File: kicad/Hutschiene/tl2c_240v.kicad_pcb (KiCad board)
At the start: 2 copper layers, 82 x 58.4 mm, 23 parts, among them P106 240VAC, P107 LED_DRIVER, P108 LED_OUT, Q401 IRLML2502, Q402 IRLML2502, Q403 IRLML2502

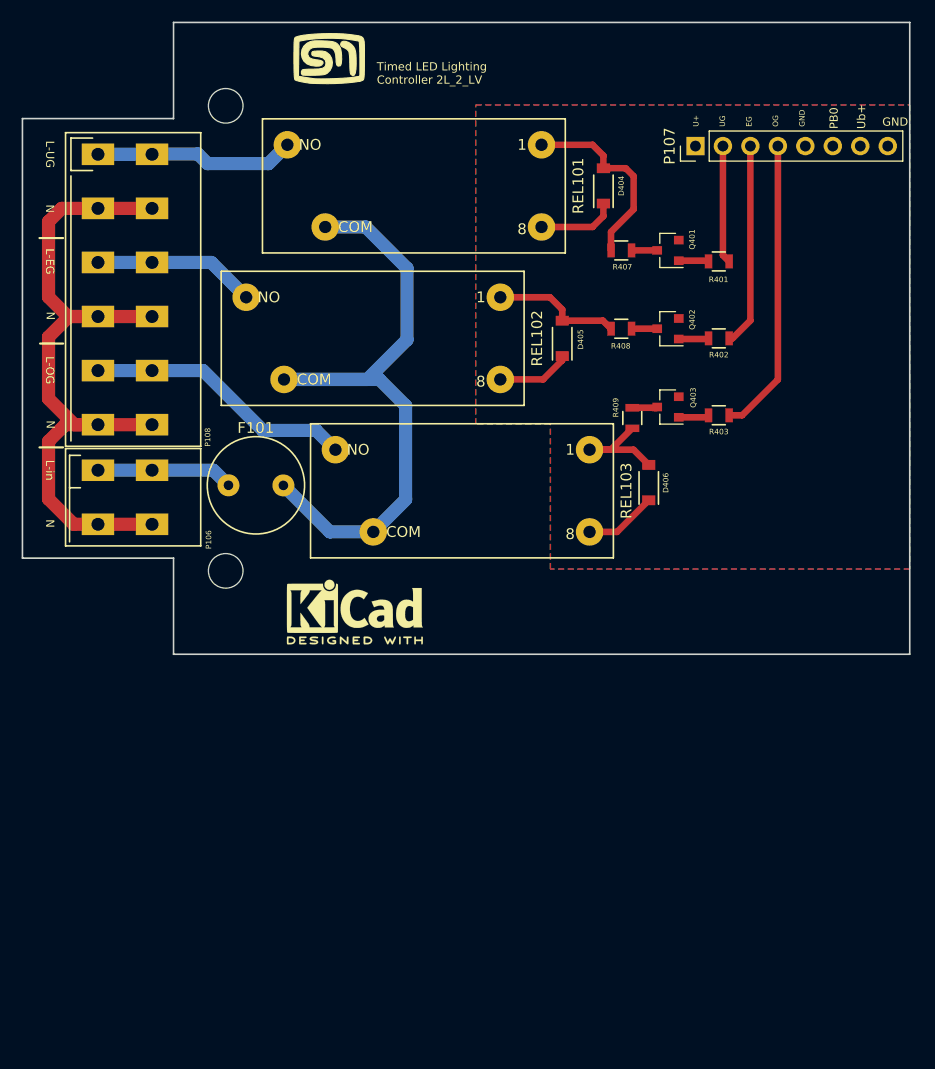
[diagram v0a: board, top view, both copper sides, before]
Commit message: Adjusted the size and location of the terminal blocks
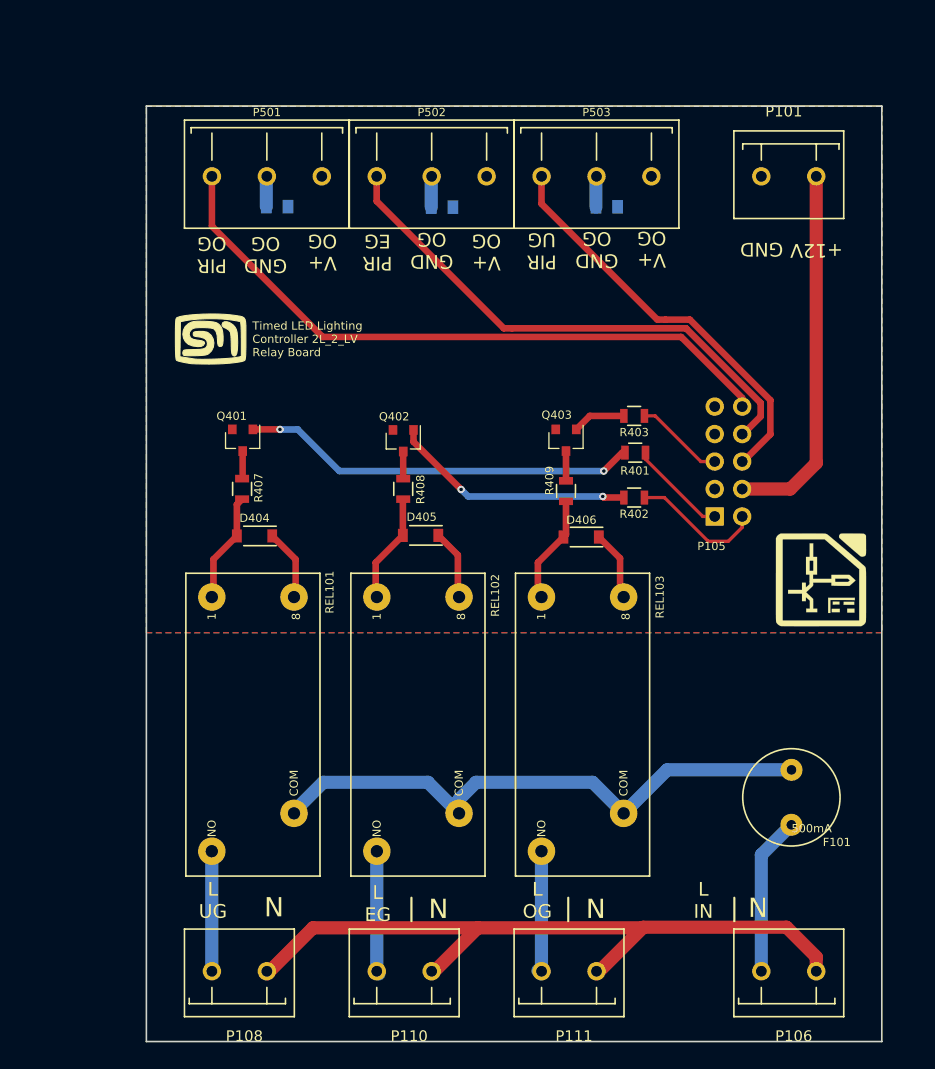
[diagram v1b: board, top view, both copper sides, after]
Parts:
- removed P107: LED_DRIVER, Pin_Headers:Pin_Header_Straight_1x08_Pitch2.54mm
- removed REF** (x2): MountingHole_3.2mm_M3, Mounting_Holes:MountingHole_3.2mm_M3
- removed REF***: KiCad-Logo2_6mm_SilkScreen, Symbols:KiCad-Logo2_6mm_SilkScreen
- added C501: 100nF 50V, Capacitors_SMD:C_0805, B.Cu at (57.8, 69.1)
- added C502: 100nF 50V, Capacitors_SMD:C_0805, B.Cu at (88.3, 69.1)
- added C503: 100nF 50V, Capacitors_SMD:C_0805, B.Cu at (73.1, 69.2)
- added G***: LOGO, tl2c-footprint:KiCad_LOGO_9mm, F.Cu at (108.1, 103.5)
- added P101: 12VDC, tl2c-footprint:PCB_Screw_Terminal_Block_5.08mm_x_2, F.Cu at (107.7, 66.3)
- added P105: DRV CONN, Pin_Headers:Pin_Header_Straight_2x05_Pitch2.54mm, B.Cu at (98.3, 97.8)
- added P110: EG, tl2c-footprint:PCB_Screw_Terminal_Block_5.08mm_x_2, F.Cu at (67.0, 139.8)
- added P111: OG, tl2c-footprint:PCB_Screw_Terminal_Block_5.08mm_x_2, F.Cu at (82.3, 139.8)
- added P501: CONN_PIR_OG, tl2c-footprint:PCB_Screw_Terminal_Block_5.8mm_x_3, F.Cu at (56.9, 66.3)
- added P502: CONN_PIR_EG, tl2c-footprint:PCB_Screw_Terminal_Block_5.8mm_x_3, F.Cu at (72.1, 66.3)
- added P503: CONN_PIR_UG, tl2c-footprint:PCB_Screw_Terminal_Block_5.8mm_x_3, F.Cu at (87.4, 66.3)
- P106: footprint tl2c-footprint:TERMINAL_BLOCK_2_5MM_5MM -> tl2c-footprint:PCB_Screw_Terminal_Block_5.08mm_x_2
- P108: value LED_OUT -> UG; footprint tl2c-footprint:TERMINAL_BLOCK_6_5MM_5MM -> tl2c-footprint:PCB_Screw_Terminal_Block_5.08mm_x_2
- moved P106 76.9 mm to (102.6, 139.8)
- moved P108 76.3 mm to (51.8, 139.8)
- moved F101 57.3 mm to (105.4, 123.7), turned to 90 degrees
- moved REL101 52.0 mm to (55.6, 117.0), turned to 90 degrees
- moved D404 45.7 mm to (55.8, 99.5), turned to 180 degrees
- moved Q401 43.1 mm to (54.6, 90.7), turned to 270 degrees
- moved R407 41.4 mm to (54.6, 95.2), turned to 90 degrees
- moved REL102 36.0 mm to (70.9, 117.0), turned to 90 degrees
- moved G*** 28.1 mm to (51.6, 81.3)
- moved Q402 26.6 mm to (69.5, 90.8), turned to 270 degrees
- moved R408 25.0 mm to (69.5, 95.2), turned to 90 degrees
- moved REL103 24.3 mm to (86.1, 117.0), turned to 90 degrees
- moved D405 22.4 mm to (71.1, 99.5), turned to 180 degrees
- moved R401 19.3 mm to (91.0, 91.8)
- moved R402 16.7 mm to (90.8, 96.0)
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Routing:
- net /PIR_Connector/PIR_OG: track 0.00 -> 61.0 mm
- net /PIR_Connector/PIR_EG: track 0.00 -> 49.7 mm
- net /PIR_Connector/PIR_UG: track 0.00 -> 38.5 mm
- net /DRV_PWR_IN: track 0.00 -> 34.4 mm
- net Net-(Q401-Pad1): track 2.78 -> 36.7 mm, vias 0 -> 2
- net Net-(Q402-Pad1): track 2.77 -> 22.7 mm, vias 0 -> 2
- net /LED Driver/Relay_OG: track 27.5 -> 8.25 mm
- net /LineOG: track 25.0 -> 11.5 mm
- net Net-(F101-Pad2): track 64.0 -> 53.3 mm
- net GNDA: track 0.00 -> 8.53 mm
- net Net-(D404-Pad2): track 18.0 -> 10.2 mm
- net /LineUG: track 18.6 -> 11.1 mm
- net /LED Driver/Relay_EG: track 18.8 -> 12.3 mm
- net /LineEG: track 15.3 -> 11.5 mm
- net /Neutral: track 70.1 -> 67.4 mm
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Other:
- board size 82 x 58.4 mm -> 68 x 86.5 mm
- copper layers 2 -> 4
- board text added: "+12V"
- board text added: "500mA"
- board text added: "GND OG"
- board text added: "L EG"
- board text added: "L IN"
- board text added: "L OG"
- board text added: "L UG"
- board text added: "PIR EG"
- board text added: "PIR OG"
- board text added: "PIR UG"
- board text added: "Timed LED Lighting Controller 2L_2_LV Relay Board"
- board text added: "V+ OG"
- board text removed: "L-EG"
- board text removed: "L-OG"
- board text removed: "L-UG"
- board text removed: "L-in"
- board text removed: "PB0"
- board text removed: "Timed LED Lighting Controller 2L_2_LV"
- board text removed: "U+ UG EG OG GND"
- board text removed: "Ub+"

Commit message: Pushed the boards to OSHPark
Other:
- copper layers 4 -> 2
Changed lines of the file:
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@@
     (links 51)
     (no_connects 0)
-    (area 20.250001 40.4 248.26 176.820001)
+    (area 45.674999 59.724999 113.825001 146.375001)
     (thickness 1.6)
     (drawings 62)
@@
   (layers
     (0 F.Cu signal)
-    (1 Ub+ power)
-    (2 U+ power)
     (31 B.Cu signal)
     (32 B.Adhes user)
@@
     (40 Dwgs.User user)
     (41 Cmts.User user)
-    (42 Eco1.User user)
-    (43 Eco2.User user)
+    (42 Eco1.User user hide)
+    (43 Eco2.User user hide)
     (44 Edge.Cuts user)
     (45 Margin user)
@@
     (at 105.39 123.72 90)
     (tags "Fuse, ESKA")
-    (fp_text reference F101 (at -4.15 4.2 180) (layer F.SilkS)
+    (fp_text reference F101 (at -4.37 5.06 180) (layer F.SilkS)
       (effects (font (size 0.762 0.762) (thickness 0.127)))
     )
@@
   (module tl2c-footprint:PCB_Screw_Terminal_Block_5.8mm_x_3 (layer F.Cu)
     (at 56.89 66.3 180)
-    (fp_text reference P501 (at 0 5.92 180) (layer F.SilkS)
+    (fp_text reference P501 (at 0.01 5.76 180) (layer F.SilkS)
       (effects (font (size 0.762 0.762) (thickness 0.127)))
     )
@@
   (module tl2c-footprint:PCB_Screw_Terminal_Block_5.8mm_x_3 (layer F.Cu)
     (at 72.13 66.3 180)
-    (fp_text reference P502 (at 0 5.92 180) (layer F.SilkS)
+    (fp_text reference P502 (at 0.01 5.76 180) (layer F.SilkS)
       (effects (font (size 0.762 0.762) (thickness 0.127)))
     )
@@
   (module tl2c-footprint:PCB_Screw_Terminal_Block_5.8mm_x_3 (layer F.Cu)
     (at 87.37 66.3 180)
-    (fp_text reference P503 (at 0 5.92 180) (layer F.SilkS)
+    (fp_text reference P503 (at 0.08 5.76 180) (layer F.SilkS)
       (effects (font (size 0.762 0.762) (thickness 0.127)))
     )
@@
   (module tl2c-footprint:PCB_Screw_Terminal_Block_5.08mm_x_2 (layer F.Cu)
     (at 102.61 139.8)
-    (fp_text reference P106 (at 3 6) (layer F.SilkS)
+    (fp_text reference P106 (at 3.08 5.06) (layer F.SilkS)
       (effects (font (size 1 1) (thickness 0.15)))
     )
@@
   (module tl2c-footprint:PCB_Screw_Terminal_Block_5.08mm_x_2 (layer F.Cu)
     (at 51.81 139.8)
-    (fp_text reference P108 (at 3 6) (layer F.SilkS)
+    (fp_text reference P108 (at 2.48 5.06) (layer F.SilkS)
       (effects (font (size 1 1) (thickness 0.15)))
     )
@@
   (module tl2c-footprint:PCB_Screw_Terminal_Block_5.08mm_x_2 (layer F.Cu)
     (at 67.05 139.8)
-    (fp_text reference P110 (at 3 6) (layer F.SilkS)
+    (fp_text reference P110 (at 3.05 5.09) (layer F.SilkS)
       (effects (font (size 1 1) (thickness 0.15)))
     )
@@
   (module tl2c-footprint:PCB_Screw_Terminal_Block_5.08mm_x_2 (layer F.Cu)
     (at 82.29 139.8)
-    (fp_text reference P111 (at 3 6) (layer F.SilkS)
+    (fp_text reference P111 (at 3.05 4.98) (layer F.SilkS)
       (effects (font (size 1 1) (thickness 0.15)))
     )
@@
   (module tl2c-footprint:PCB_Screw_Terminal_Block_5.08mm_x_2 (layer F.Cu)
     (at 107.69 66.3 180)
-    (fp_text reference P101 (at 3 6 180) (layer F.SilkS)
+    (fp_text reference P101 (at 2.42 5 180) (layer F.SilkS)
       (effects (font (size 1 1) (thickness 0.15)))
     )
@@
     (arrow2b (pts (xy 28.25 59.8) (xy 28.836421 60.926504)))
   )
-  (gr_text 500mA (at 105.4 126.6) (layer F.SilkS)
+  (gr_text 500mA (at 103.9 118.53) (layer F.SilkS)
     (effects (font (size 0.762 0.762) (thickness 0.127)) (justify left))
   )
-  (gr_text GND (at 102.64 73.04 180) (layer F.SilkS)
+  (gr_text GND (at 102.45 71.36 180) (layer F.SilkS)
     (effects (font (size 1.27 1.27) (thickness 0.1778)))
   )
-  (gr_text +12V (at 107.71 73.15 180) (layer F.SilkS)
+  (gr_text +12V (at 108.17 71.21 180) (layer F.SilkS)
     (effects (font (size 1.27 1.27) (thickness 0.1778)))
   )
@@
     (effects (font (size 1.27 1.27) (thickness 0.1778)))
   )
-  (gr_text "L\nIN" (at 97.25 133.25) (layer F.SilkS)
+  (gr_text "L\nIN" (at 102.4 133.25) (layer F.SilkS)
     (effects (font (size 1.27 1.27) (thickness 0.1778)))
   )
@@
     (effects (font (size 1.27 1.27) (thickness 0.1778)))
   )
-  (gr_text N (at 102.3 133.95) (layer F.SilkS)
+  (gr_text N (at 107.54 134.06) (layer F.SilkS)
     (effects (font (size 1.778 1.778) (thickness 0.254)))
   )
@@
   (gr_line (start 45.75 146.3) (end 45.75 59.8) (angle 90) (layer Edge.Cuts) (width 0.15))
   (gr_line (start 70.259 133.0008) (end 70.259 135.1852) (angle 90) (layer F.SilkS) (width 0.2))
-  (gr_line (start 100.1138 133.0008) (end 100.1138 135.1852) (angle 90) (layer F.SilkS) (width 0.2))
+  (gr_line (start 105.1138 132.9208) (end 105.1138 135.1052) (angle 90) (layer F.SilkS) (width 0.2))
   (gr_text "L\nEG" (at 67.15 133.55) (layer F.SilkS)
     (effects (font (size 1.27 1.27) (thickness 0.1778)))

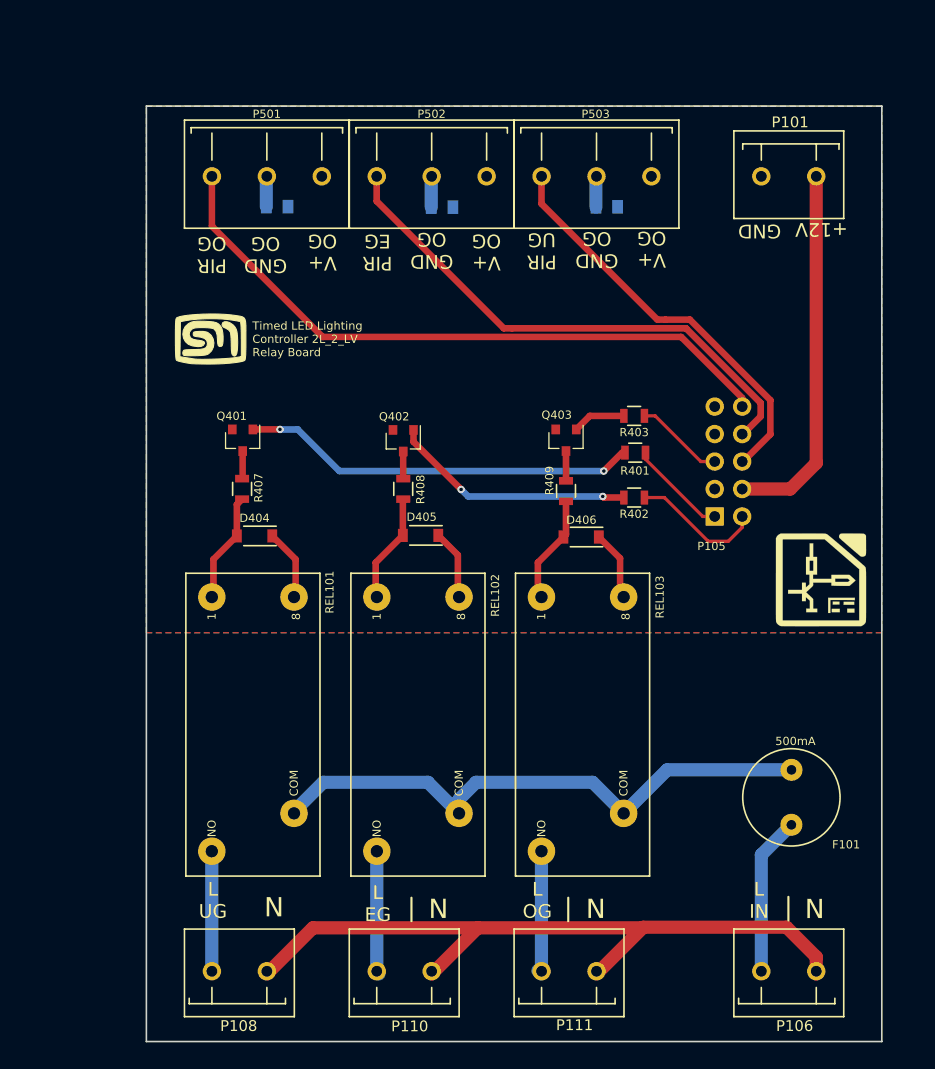
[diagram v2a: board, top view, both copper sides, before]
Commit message: Corrections to the terminal block drill holes
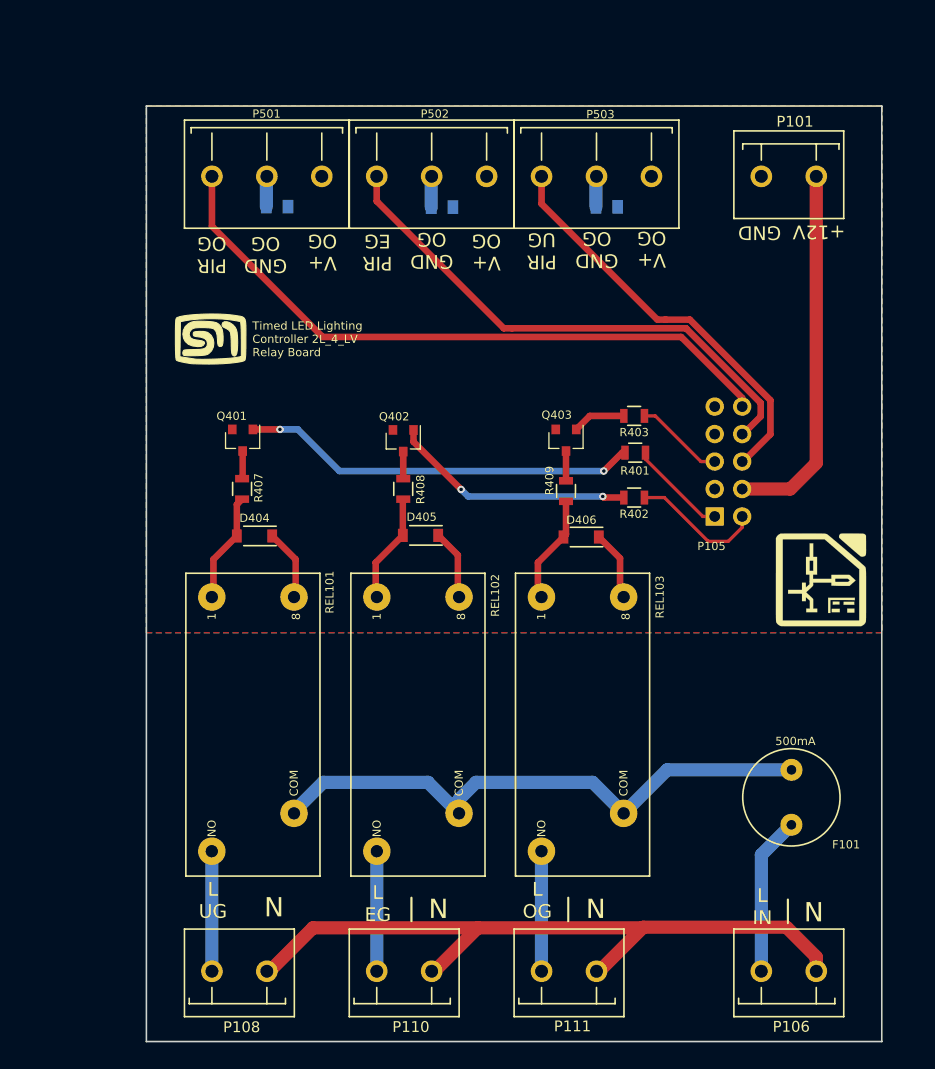
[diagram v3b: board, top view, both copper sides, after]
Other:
- board text added: "Timed LED Lighting Controller 2L_4_LV Relay Board"
- board text removed: "Timed LED Lighting Controller 2L_2_LV Relay Board"

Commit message: Correction to the board connected and seperated out the pwr
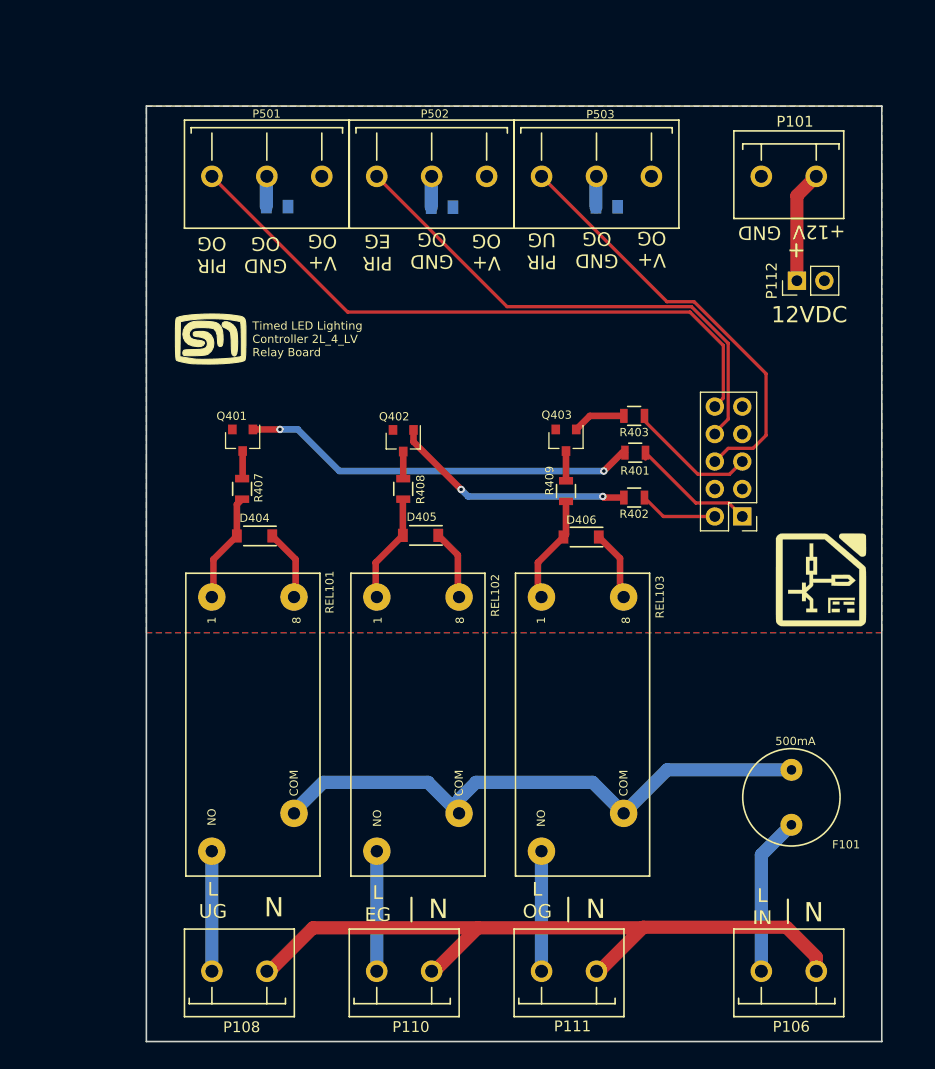
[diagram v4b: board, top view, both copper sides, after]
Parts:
- added P112: DRV PWR, Pin_Headers:Pin_Header_Straight_1x02_Pitch2.54mm, F.Cu at (105.9, 76.0)
- P105: moved to F.Cu
- moved P105 2.55 mm to (100.8, 97.8), turned to 180 degrees
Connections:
- P105 pad 4: /DRV_PWR_IN -> (no net)
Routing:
- net /DRV_PWR_IN: track 34.4 -> 10.4 mm
- net /LED Driver/Relay_EG: track 12.3 -> 7.23 mm
- net /LED Driver/Relay_OG: track 8.25 -> 12.5 mm
- net /LED Driver/Relay_UG: track 9.20 -> 12.0 mm
- net /PIR_Connector/PIR_EG: track 49.7 -> 47.8 mm
- net /PIR_Connector/PIR_UG: track 38.5 -> 40.0 mm
- net /PIR_Connector/PIR_OG: track 61.0 -> 59.7 mm
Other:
- board text added: "+"
- board text added: "12VDC"

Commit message: Corrected issues with the connectors - Pushing to OSH Park
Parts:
- added R404: 10kΩ, Resistors_SMD:R_0805, F.Cu at (110.1, 97.8)
- added R405: 10kΩ, Resistors_SMD:R_0805, F.Cu at (99.8, 101.9)
- added R406: 10kΩ, Resistors_SMD:R_0805, F.Cu at (110.1, 92.7)
- C501, C502, C503: footprint Capacitors_SMD:C_0805 -> Capacitors_SMD:C_0805_HandSoldering
- P105: footprint Pin_Headers:Pin_Header_Straight_2x05_Pitch2.54mm -> Socket_Strips:Socket_Strip_Straight_2x05_Pitch2.54mm
- R401, R402, R403, R407, R408, R409: value 10kΩ -> 0kΩ
- moved R401 34.5 mm to (56.9, 85.8)
- moved R402 21.6 mm to (71.8, 85.8)
- moved G*** 4.84 mm to (108.5, 108.3)
- moved R403 4.82 mm to (86.8, 85.8)
- moved P105 2.55 mm to (98.3, 97.8)
- moved C501 0.50 mm to (58.1, 69.5)
- moved C502 0.48 mm to (88.6, 69.5)
- moved C503 0.45 mm to (73.4, 69.5)
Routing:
- net /LED Driver/Relay_UG: track 12.0 -> 58.3 mm, vias 0 -> 1
- net /LED Driver/Relay_EG: track 7.23 -> 40.4 mm, vias 0 -> 1
- net Net-(Q401-Pad1): track 36.7 -> 4.10 mm, vias 2 -> 0
- net Net-(Q402-Pad1): track 22.7 -> 4.15 mm, vias 2 -> 0
- net /LED Driver/Relay_OG: track 12.5 -> 25.9 mm
- net /PIR_Connector/PIR_OG: track 59.7 -> 70.0 mm
- net /PIR_Connector/PIR_EG: track 47.8 -> 56.6 mm
- net /PIR_Connector/PIR_UG: track 40.0 -> 47.1 mm
- net GNDA: track 8.53 -> 9.78 mm
- net Net-(Q403-Pad1): track 4.92 -> 4.11 mm
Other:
- board text added: "GND EG"
- board text added: "GND PB2 Rly OG V+ Rly UG"
- board text added: "GND UG"
- board text added: "PIR OG PIR EG PIR UG NC Rly EG"
- board text added: "V+ EG"
- board text added: "V+ UG"
